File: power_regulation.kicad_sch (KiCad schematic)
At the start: 71 parts, among them J1 Conn_01x02, J2 Conn_02x01, J3 Conn_02x01, K1 G5Q-1A DC24, Q1 BSS138, Q12 BSS138, Q2 BSS138, Q3 DMP6023LE-13, U1 LM3880-1AA, U2 LMR33630BDDA, U3 TPS78533QKVURQ1, U4 TLC555xPS, U5 TPS78450QDBVRQ1, U6 LM66200DRLR

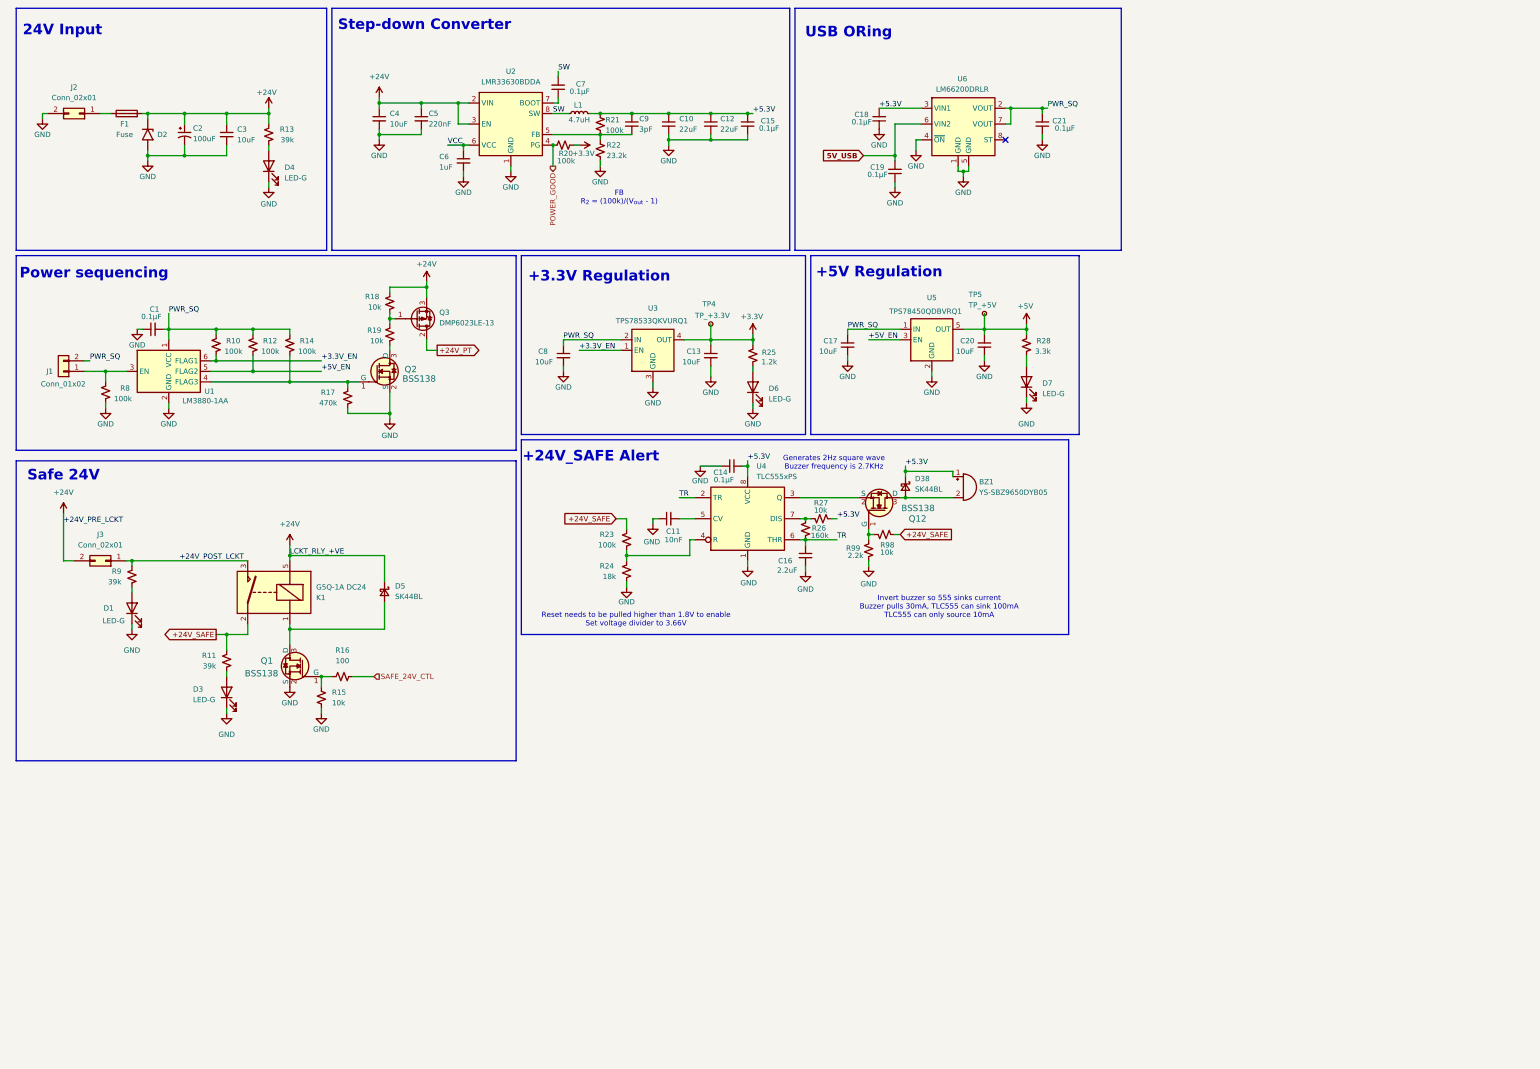
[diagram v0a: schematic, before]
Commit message: remove remainder of leftofer schematics
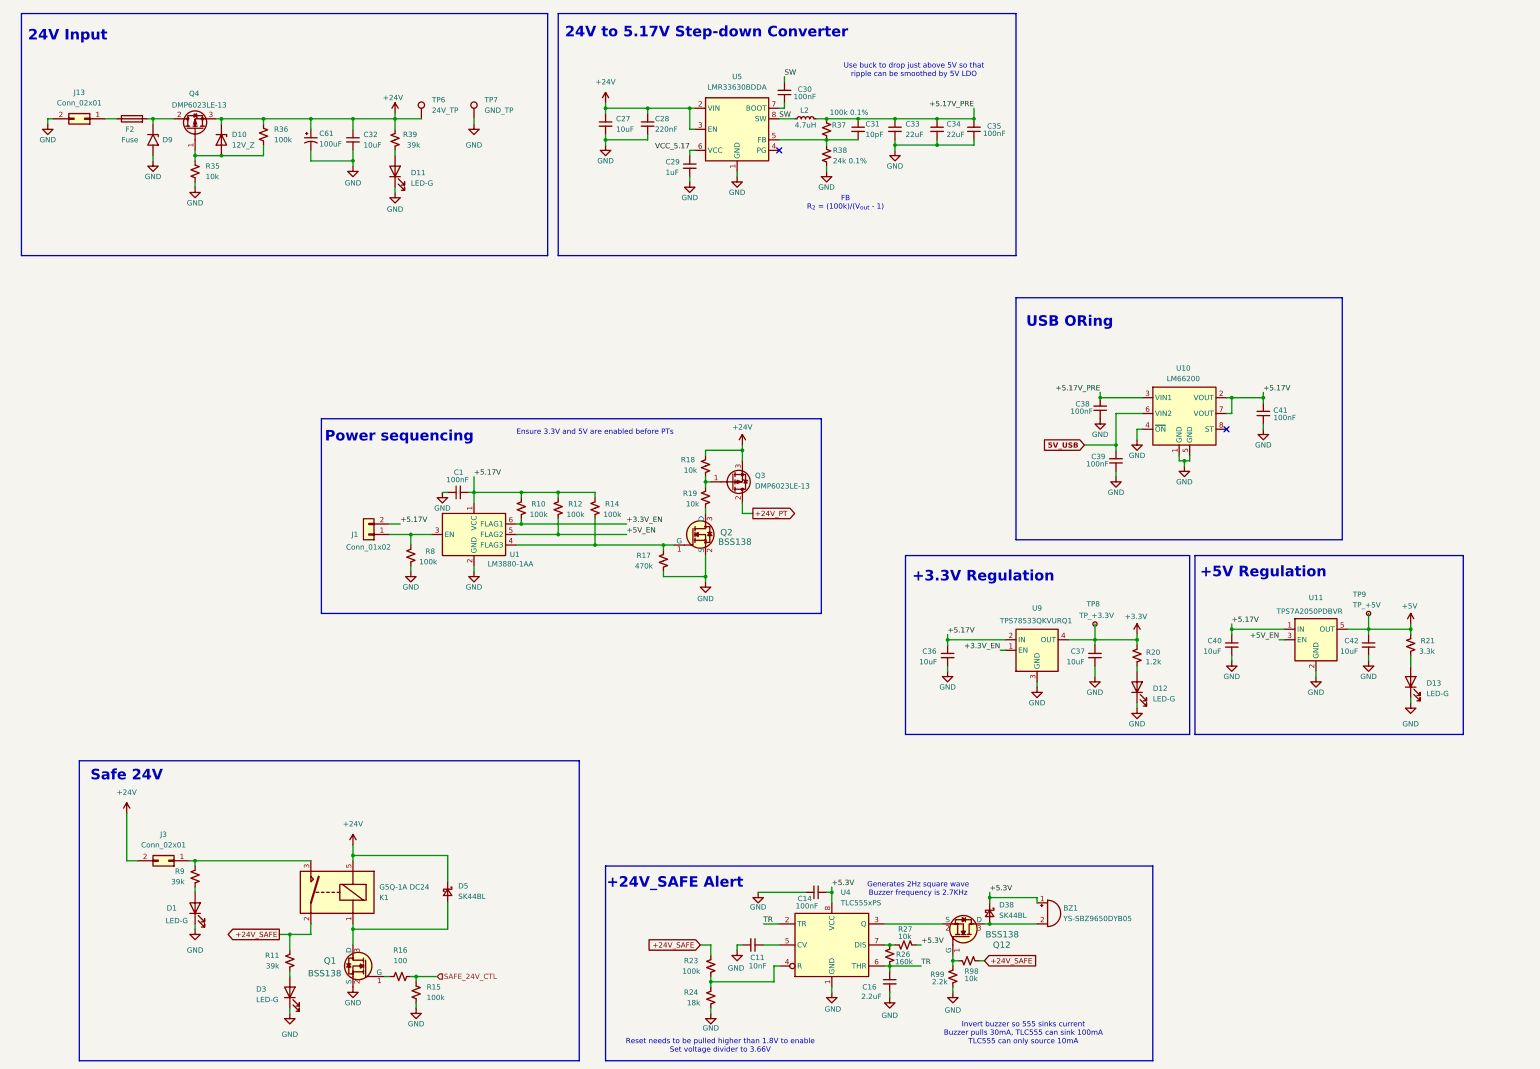
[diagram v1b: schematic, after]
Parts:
- removed C10, C12: 22uF, Capacitor_SMD:C_0805_2012Metric, symbol Device:C_Small
- removed C13, C17, C20, C8: 10uF, Capacitor_SMD:C_0805_2012Metric, symbol Device:C_Small
- removed C15, C18, C19, C21, C7: 0.1μF, Capacitor_SMD:C_0402_1005Metric, symbol Device:C_Small
- removed C2: 100uF, Capacitor_SMD:CP_Elec_10x10, symbol Device:C_Polarized_Small_US
- removed C3: 10uF, Capacitor_SMD:C_1812_4532Metric, symbol Device:C_Small
- removed C4: 10uF, Capacitor_SMD:C_1206_3216Metric, symbol Device:C_Small
- removed C5: 220nF, Capacitor_SMD:C_0805_2012Metric, symbol Device:C_Small
- removed C6: 1uF, Capacitor_SMD:C_0603_1608Metric, symbol Device:C_Small
- removed C9: 3pF, Capacitor_SMD:C_0603_1608Metric, symbol Device:C_Small
- removed D2: SMCJ26A-13-F, Diode_SMD:D_SMC, symbol Diode:1.5SMCxxA
- removed D4, D6, D7: LED-G, LED_SMD:LED_0805_2012Metric, symbol Device:LED
- removed F1: Fuse, Fuse:Fuseholder_Blade_Mini_Keystone_3568, symbol Device:Fuse
- removed J2: Conn_02x01, Connector_Molex:Molex_Mini-Fit_Jr_5566-02A_2x01_P4.20mm_Vertical, symbol Connector_Generic:Conn_02x01
- removed L1: 4.7uH, Inductor_SMD:L_Bourns_SRP7028A_7.3x6.6mm, symbol Device:L_Small
- removed R13: 39k, Resistor_SMD:R_0402_1005Metric, symbol Device:R_Small_US
- removed R22: 23.2k, Resistor_SMD:R_0603_1608Metric, symbol Device:R_Small_US
- removed R25: 1.2k, Resistor_SMD:R_0402_1005Metric, symbol Device:R_Small_US
- removed R28: 3.3k, Resistor_SMD:R_0402_1005Metric, symbol Device:R_Small_US
- removed TP4: TP_+3.3V, TestPoint:TestPoint_Pad_D1.0mm, symbol Connector:TestPoint_Small
- removed TP5: TP_+5V, TestPoint:TestPoint_Pad_D1.0mm, symbol Connector:TestPoint_Small
- removed U2: LMR33630BDDA, Package_SO:Texas_HSOP-8-1EP_3.9x4.9mm_P1.27mm_ThermalVias, symbol Regulator_Switching:LMR33630BDDA
- removed U3: TPS78533QKVURQ1, Package_TO_SOT_SMD:TO-252-4, symbol Regulator_Linear:TPS78236DDC
- removed U5: TPS78450QDBVRQ1, Package_TO_SOT_SMD:SOT-23-5, symbol Regulator_Linear:TPS78236DDC
- removed U6: LM66200DRLR, Package_TO_SOT_SMD:SOT-583-8, symbol LM66200DRLR:LM66200DRLR
- added C27: 10uF, Capacitor_SMD:C_1206_3216Metric, symbol Device:C_Small
- added C28: 220nF, Capacitor_SMD:C_0805_2012Metric, symbol Device:C_Small
- added C29: 1uF, Capacitor_SMD:C_0603_1608Metric, symbol Device:C_Small
- added C30, C35: 100nF, Capacitor_SMD:C_0402_1005Metric, symbol Device:C_Small
- added C31: 10pF, Capacitor_SMD:C_0603_1608Metric, symbol Device:C_Small
- added C32, C36, C37, C40, C42: 10uF, symbol Device:C_Small
- added C33, C34: 22uF, Capacitor_SMD:C_0805_2012Metric, symbol Device:C_Small
- added C38, C39, C41: 100nF, symbol Device:C_Small
- added C61: 100uF, Capacitor_THT:CP_Radial_D8.0mm_P5.00mm, symbol Device:C_Polarized_Small_US
- added D10: 12V_Z, Diode_SMD:D_SOD-123, symbol Device:D_Zener
- added D11, D12, D13: LED-G, LED_SMD:LED_0805_2012Metric, symbol Device:LED
- added D9: SMCJ26A-13-F, Diode_SMD:D_SMC, symbol Diode:1.5SMCxxA
- added F2: Fuse, Fuse:Fuseholder_Blade_Mini_Keystone_3568, symbol Device:Fuse
- added J13: Conn_02x01, Connector_Molex:Molex_Mini-Fit_Jr_5566-02A_2x01_P4.20mm_Vertical, symbol Connector_Generic:Conn_02x01
- added L2: 4.7uH, Inductor_SMD:L_Bourns_SRP7028A_7.3x6.6mm, symbol Device:L_Small
- added Q4: DMP6023LE-13, Package_TO_SOT_SMD:SOT-223-3_TabPin2, symbol Transistor_FET:ZXMP4A16G
- added R35: 10k, symbol Device:R_Small_US
- added R36: 100k, symbol Device:R_Small_US
- added R37: 100k 0.1%, Resistor_SMD:R_0603_1608Metric, symbol Device:R_Small_US
- added R38: 24k 0.1%, Resistor_SMD:R_0603_1608Metric, symbol Device:R_Small_US
- added R39: 39k, symbol Device:R_Small_US
- added TP6: 24V_TP, TestPoint:TestPoint_Loop_D2.50mm_Drill1.0mm, symbol Connector:TestPoint
- added TP7: GND_TP, TestPoint:TestPoint_Loop_D2.50mm_Drill1.0mm, symbol Connector:TestPoint
- added TP8: TP_+3.3V, TestPoint:TestPoint_Pad_D1.0mm, symbol Connector:TestPoint_Small
- added TP9: TP_+5V, TestPoint:TestPoint_Pad_D1.0mm, symbol Connector:TestPoint_Small
- added U10: LM66200, Package_TO_SOT_SMD:SOT-583-8, symbol LM66200DRLR:LM66200DRLR
- added U11: TPS7A2050PDBVR, Package_TO_SOT_SMD:SOT-23-5, symbol Regulator_Linear:TPS78236DDC
- added U5: LMR33630BDDA, Package_SO:Texas_HSOP-8-1EP_3.9x4.9mm_P1.27mm_ThermalVias, symbol Regulator_Switching:LMR33630BDDA
- added U9: TPS78533QKVURQ1, Package_TO_SOT_SMD:TO-252-4, symbol Regulator_Linear:TPS78236DDC
- C1, C14: value 0.1μF -> 100nF; footprint Capacitor_SMD:C_0402_1005Metric -> (none); LCSC C307331 -> (none); MPN CL05B104KO5NNNC -> (none)
- C11: footprint Capacitor_SMD:C_0402_1005Metric -> (none); Dielectric X5R or X7R -> (none); LCSC C15195 -> (none)
- C16: footprint Capacitor_SMD:C_0603_1608Metric -> (none); Dielectric X5R or X7R -> (none); LCSC C23630 -> (none)
- Q1, Q12, Q2: Category Discrete Semiconductor Products -> (none); DK_Datasheet_Link https://www.onsemi.com/pub/Collateral/BSS138-D.PDF -> (none); DK_Detail_Page /product-detail/en/on-semiconductor/BSS138/BSS138CT-ND/2442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 -> (none); Description_1 MOSFET N-CH 50V 220MA SOT-23 -> (none); Family Transistors - FETs, MOSFETs - Single -> (none); Manufacturer ON Semiconductor -> (none); Status Active -> (none)
- R10, R12, R14, R17, R23, R24, R8: footprint Resistor_SMD:R_0603_1608Metric -> (none)
- R11, R18, R19, R26, R27, R9, R98, R99: footprint Resistor_SMD:R_0402_1005Metric -> (none)
- R15: value 10k -> 100k; footprint Resistor_SMD:R_0402_1005Metric -> (none); LCSC C25531 -> (none); MPN 0402WGJ0103TCE -> (none)
- R16: footprint Resistor_SMD:R_0402_1005Metric -> (none); LCSC C25076 -> (none); MPN 0402WGF1000TCE -> (none)
- R20: value 100k -> 1.2k; footprint Resistor_SMD:R_0603_1608Metric -> (none); LCSC C25531 -> (none); MPN 0402WGJ0103TCE -> (none)
- R21: value 100k -> 3.3k; footprint Resistor_SMD:R_0603_1608Metric -> (none); LCSC C25531 -> (none); MPN 0402WGJ0103TCE -> (none)
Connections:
- net +24V: now also C27.1, C28.1, C32.1, C61.1, D10.1 (K), Q4.3 (S), R36.1, R39.2, TP6.1, U5.2 (VIN), U5.3 (EN)
- net +3.3V: now also C37.1, TP8.1, U9.4 (OUT)
- net +3.3V_EN: now also U9.1 (EN)
- net +5.3V: no longer R21.1
- net +5V: now also R21.2, C42.1, TP9.1, U11.5 (OUT)
- net +5V_EN: now also U11.3 (EN)
- net 5V_USB: now also C39.2, U10.6 (VIN2)
- net GND: now also C27.2, C28.2, C29.2, C32.2, C33.2, C34.2, C35.1, C36.2, C37.2, C38.1, C39.1, C40.2, C41.1, C42.2, C61.2, D11.1 (K), D12.1 (K), D13.1 (K), D9.2 (A2), J13.2 (Pin_2), R35.2, R38.2, TP7.1, U10.1 (GND), U10.4 (~{ON}), U10.5 (GND), U11.2 (GND), U5.1 (GND), U5.9 (GND), U9.3 (GND)
- net SAFE_24V_CTL: now also R15.1
- net SW: now also C30.2, L2.1, U5.8 (SW)
- net at Q1.1 (G), R16.1: no longer R15.1
- net +24V_POST_LCKT: no longer names the net of J3.1 (Pin_1), K1.3, R9.2
- net POWER_GOOD: no longer names the net of R20.1
- net POWER_GOOD: now also D12.2 (A)
- net PWR_SQ renamed +5.17V
- net +5.17V: now also C36.1, C40.1, C41.2, U10.2 (VOUT), U10.7 (VOUT), U11.1 (IN), U9.2 (IN)
- new net: D13.2 (A), R21.1
- new net: D11.2 (A), R39.1
- new net: C31.2, R37.2, R38.1, U5.5 (FB)
- new net: D9.1 (A1), F2.2, Q4.2 (D)
- new net: D10.2 (A), Q4.1 (G), R35.1, R36.2
- new net: C30.1, U5.7 (BOOT)
- new net: F2.1, J13.1 (Pin_1)
- new net +5.17V_PRE: C31.1, C33.1, C34.1, C35.2, C38.2, L2.2, R37.1, U10.3 (VIN1)
- new net VCC_5.17: C29.1, U5.6 (VCC)
- no-connect marks 1 -> 2
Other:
- note added: "24V to 5.17V Step-down Converter"
- note added: "Ensure 3.3V and 5V are enabled before PTs"
- note added: "Use buck to drop just above 5V so that ripple can be smoothed by 5V LDO"
- note removed: "Step-down Converter"
- moved on the sheet: BZ1, C1, C11, C14, C16, D1, D3, D38, D5, J1, J3, K1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

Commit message: add afe for pressure transducers
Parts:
- removed BZ1: YS-SBZ9650DYB05, Library:YS-SBZ9650DYB05, symbol Device:Buzzer
- removed C11: 10nF, symbol Device:C_Small
- removed C14: 100nF, symbol Device:C_Small
- removed C16: 2.2uF, symbol Device:C_Small
- removed D38: SK44BL, Diode_SMD:D_SMB, symbol Device:D_Schottky_Small
- removed Q12: BSS138, Package_TO_SOT_SMD:SOT-23-3, symbol dk_Transistors-FETs-MOSFETs-Single:BSS138
- removed R23: 100k, symbol Device:R_Small_US
- removed R24: 18k, symbol Device:R_Small_US
- removed R26: 160k, symbol Device:R_Small_US
- removed R27, R98: 10k, symbol Device:R_Small_US
- removed R99: 2.2k, symbol Device:R_Small_US
- removed U4: TLC555xPS, Package_SO:VSSOP-8_3x3mm_P0.65mm, symbol Timer:TLC555xPS
- renumbered C61 to C1, C31 to C10, C33 to C12, C34 to C13, C36 to C14, C35 to C15, C37 to C16, C38 to C17, C39 to C18, C40 to C19, C32 to C2, C41 to C20, C42 to C21, C1 to C3, C27 to C4, C28 to C5, C29 to C6, C30 to C8, D9 to D1, D1 to D2, D10 to D3, D3 to D4, D11 to D5, D5 to D6, D12 to D8, D13 to D9, F2 to F1, J13 to J1, J3 to J2, J1 to J3, L2 to L1, Q4 to Q1, Q1 to Q2, Q2 to Q3, Q3 to Q4, R35 to R1, R12 to R10, R14 to R11, R17 to R12, R18 to R13, R19 to R14, R37 to R17, R38 to R18, R9 to R2, R20 to R23, R21 to R24, R36 to R3, R11 to R4, R39 to R5, R16 to R6, R8 to R7, R15 to R8, R10 to R9, TP6 to TP1, TP7 to TP2, TP8 to TP3, TP9 to TP4, U5 to U2, U9 to U4, U10 to U5, U11 to U6
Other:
- note removed: "+24V_SAFE Alert"
- note removed: "Generates 2Hz square wave Buzzer frequency is 2.7KHz"
- note removed: "Invert buzzer so 555 sinks current Buzzer pulls 30mA, TLC555 can sink 100mA TLC555 can only source 10mA"
- note removed: "Reset needs to be pulled higher than 1.8V to enable Set voltage divider to 3.66V"
- moved on the sheet: C14, C16, C17, C18, C19, C20, C21, C3, D8, D9, J3, Q3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
